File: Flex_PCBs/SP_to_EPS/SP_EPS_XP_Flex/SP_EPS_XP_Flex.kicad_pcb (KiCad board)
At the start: 2 copper layers, 4.5 x 100 mm, 2 parts, among them J1 Conn_01x08_Male, J2 Conn_01x08_Male

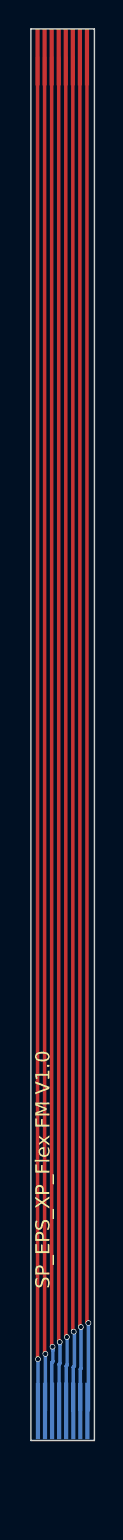
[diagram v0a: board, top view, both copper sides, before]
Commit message: Update the EPS FlexPCBs, with correct top/down and crossed out
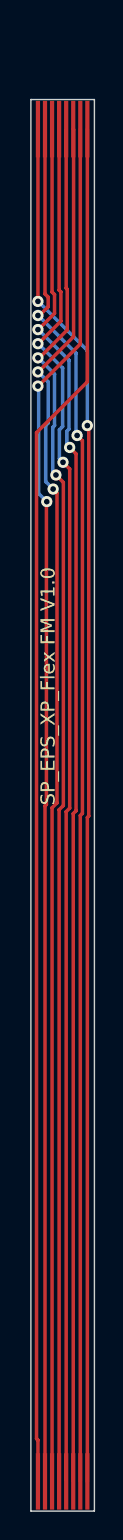
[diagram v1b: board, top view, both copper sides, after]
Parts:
- J2: moved to F.Cu
- moved J2 6.72 mm to (120.0, 154.9), turned to 0 degrees
- moved J1 5.10 mm to (120.0, 59.1)
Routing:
- net 5: track 95.9 -> 97.8 mm, vias 1 -> 2
- net 3: track 96.0 -> 97.7 mm, vias 1 -> 2
- net 6: track 96.0 -> 97.7 mm, vias 1 -> 2
- net 7: track 96.0 -> 97.6 mm, vias 1 -> 2
- net 4: track 96.1 -> 97.7 mm, vias 1 -> 2
- net 8: track 95.9 -> 97.3 mm, vias 1 -> 2
- net 1: track 96.0 -> 97.3 mm, vias 1 -> 0
- net 2: track 96.1 -> 97.4 mm, vias 1 -> 2
